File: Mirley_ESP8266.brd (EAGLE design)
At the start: 52 x 69.4 mm, 82 parts, among them J1 61301611121, J10 61300511121, J2 61301611121, J3 61300211121, J6 61300811121, J8 61300811121, T1 BC817U, T10 BC817U, T11 BC817U, T12 BC817U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

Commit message: board chagned
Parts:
- added R57: 47K, rcl:R0805
- moved J8 104.9 mm to (-45.7, 80.0), turned to 0 degrees
- moved J10 102.4 mm to (-64.8, 80.0), turned to 0 degrees
- moved U$4 96.3 mm to (-67.3, 10.2), turned to 0 degrees
- moved R11 79.0 mm to (-16.5, 114.3)
- moved U$1 66.7 mm to (-29.2, 44.5)
- moved ESP_2 66.4 mm to (-33.0, 20.3), turned to 0 degrees
- moved J6 64.2 mm to (-24.1, 80.0), turned to 0 degrees
- moved J2 46.6 mm to (2.62, 33.2), flipped to the top
- moved J1 46.5 mm to (49.1, 33.0), flipped to the top
- moved R59 6.35 mm to (-80.0, 108.0)
- moved C3 6.35 mm to (-29.2, 114.3)
- moved C1 6.35 mm to (-22.9, 114.3)
- moved C2 6.35 mm to (-34.3, 114.3)
- moved C4 6.35 mm to (-39.4, 114.3)
- moved R1 6.35 mm to (-91.4, 108.0)
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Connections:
- removed net N$10: J10.1
- net +3V3: now also R57.2
- net ENABLE: now also J10.2
- net GND: no longer J10.2
- net RESET: now also J10.1
- net TXD: now also R57.1

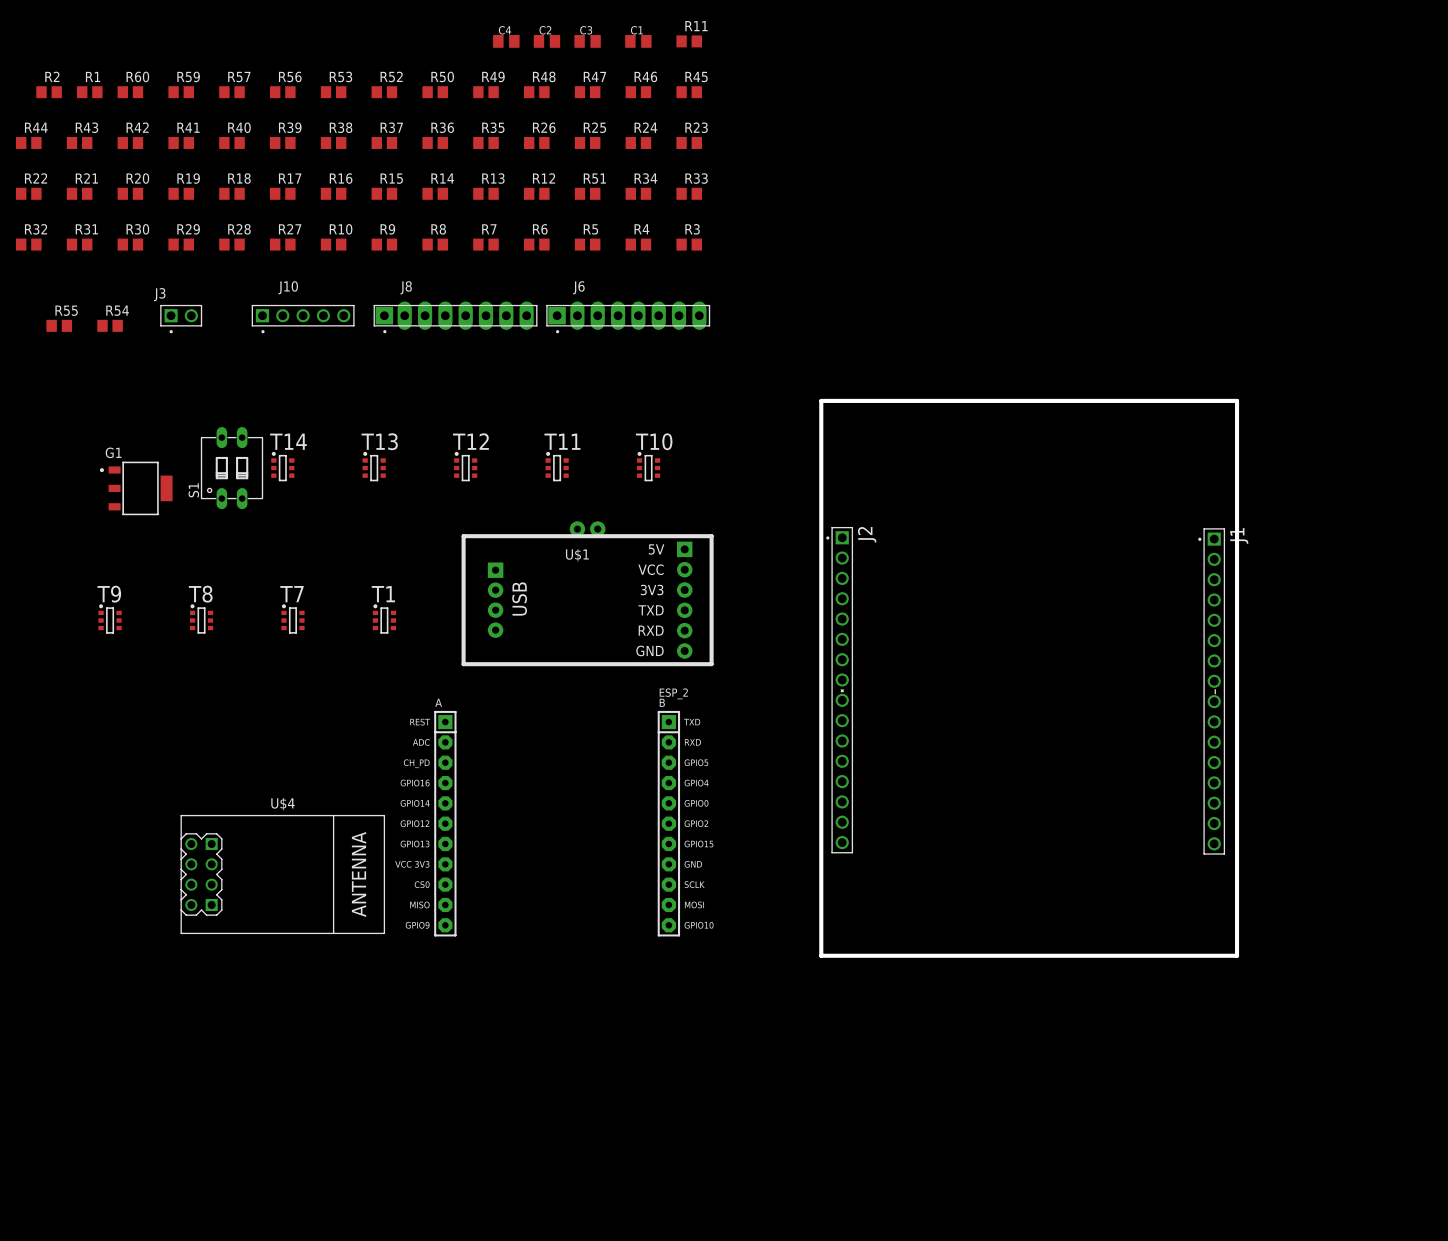
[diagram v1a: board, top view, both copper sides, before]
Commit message: pierwsza wersja na jedenj plytce, niedokonczona
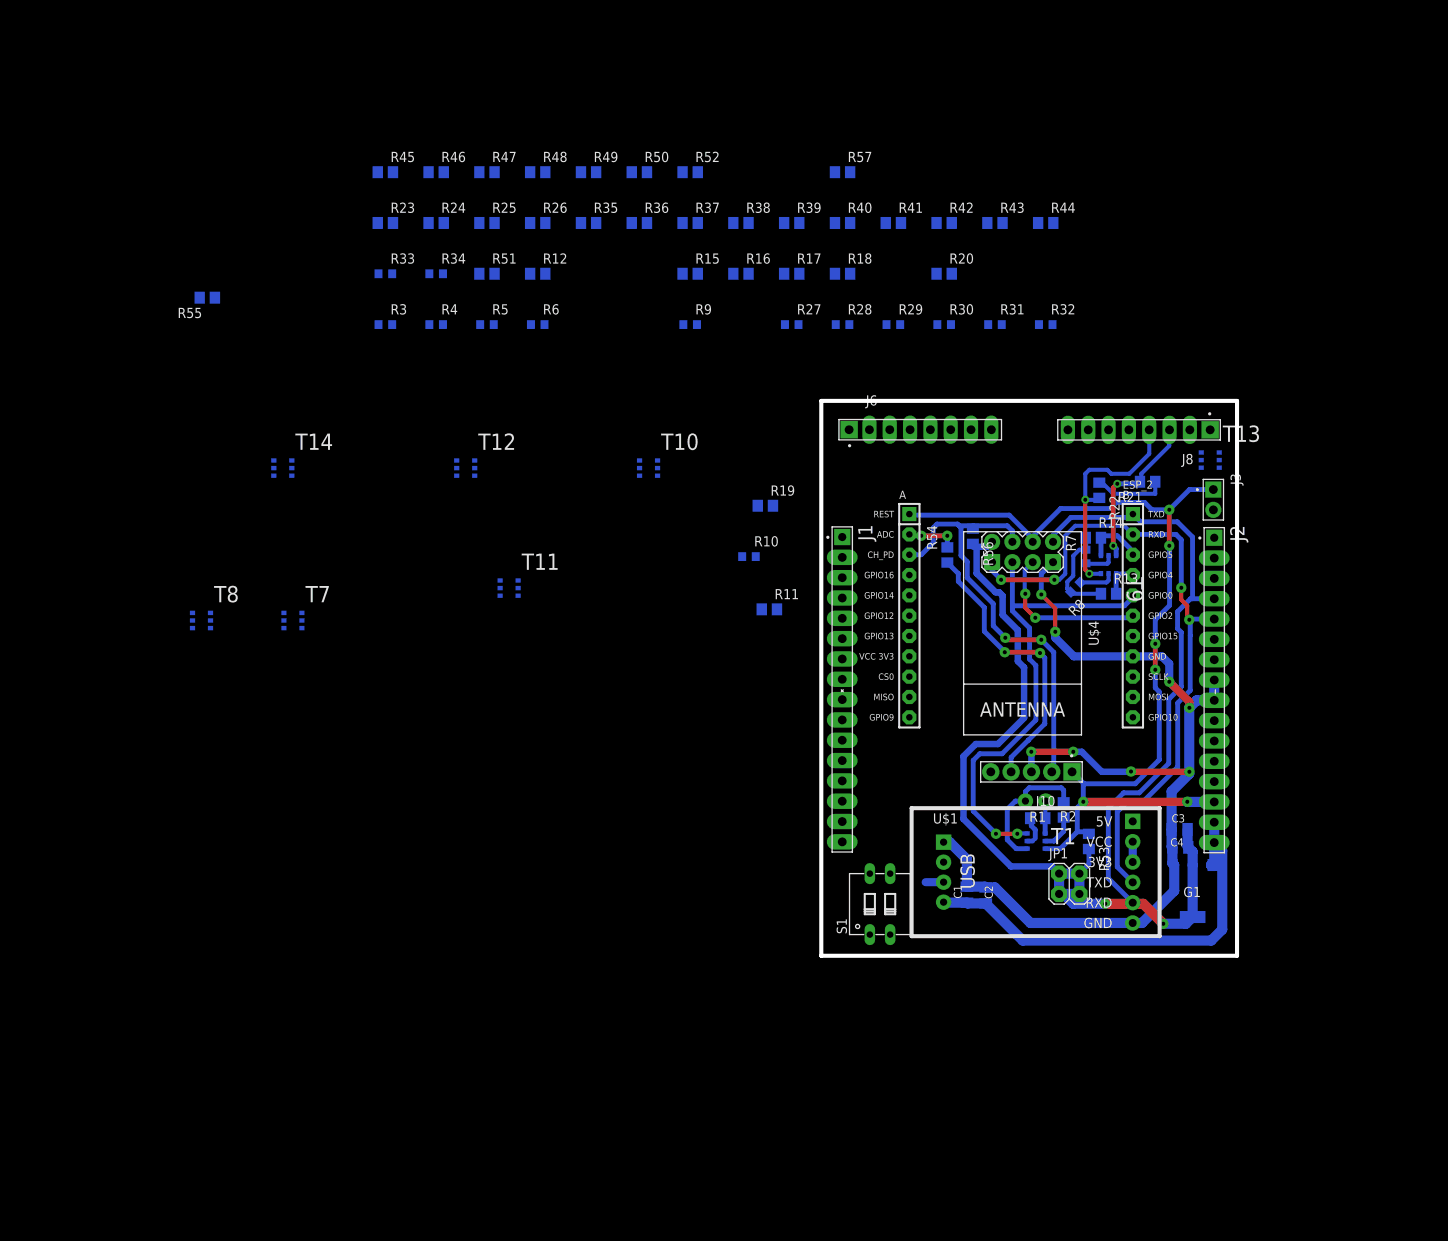
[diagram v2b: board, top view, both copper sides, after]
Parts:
- removed R59, R60: 10K, rcl:R0805
- added JP1: (no value), pinhead:2X02
- R10, R27, R28, R29, R3, R30, R31, R32, R33, R34, R4, R5, R6, R7, R8, R9: device rcl:R0805 -> rcl:R0603
- moved R2 155.3 mm to (30.3, 18.2), flipped to the bottom, turned to 90 degrees
- moved R1 149.3 mm to (27.1, 17.2), flipped to the bottom
- moved G1 140.8 mm to (46.4, 8.09), flipped to the bottom, turned to 270 degrees
- moved R22 138.8 mm to (34.8, 58.2), flipped to the bottom, turned to 90 degrees
- moved R21 138.3 mm to (40.8, 59.2), flipped to the bottom, turned to 180 degrees
- moved R53 133.0 mm to (33.5, 14.3), flipped to the bottom, turned to 90 degrees
- moved C4 131.3 mm to (44.9, 13.6), flipped to the bottom
- moved J3 131.1 mm to (49.0, 57.0), turned to 270 degrees
- moved R32 127.5 mm to (28.1, 78.9), flipped to the bottom
- moved R44 127.5 mm to (28.1, 91.6), flipped to the bottom
- moved T9 125.0 mm to (35.9, 48.9), flipped to the bottom, turned to 90 degrees
- moved C3 123.2 mm to (44.8, 15.8), flipped to the bottom
- moved C2 120.0 mm to (20.6, 7.54), flipped to the bottom, turned to 90 degrees
- moved R31 114.9 mm to (21.7, 78.9), flipped to the bottom
- moved R43 114.9 mm to (21.7, 91.6), flipped to the bottom
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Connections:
- removed net ACD0: ESP_2.2
- removed net ADC0: J10.4, R54.1, R54.2, R55.2
- new net ADC: ESP_2.2, R54.1, R55.2
- new net N$10: J10.4, R54.2
- new net N$5: U$1.3V3, U$1.VCC
- net +3V3: now also JP1.1, JP1.2, JP1.3, JP1.4; no longer R59.1, R60.1
- net ENABLE: no longer R60.2
- net RESET: no longer R59.2
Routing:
- net GND: track 0.00 -> 124.5 mm, vias 0 -> 8
- net RESET: track 0.00 -> 117.0 mm, vias 0 -> 6
- net +3V3: track 0.00 -> 115.2 mm, vias 0 -> 2
- net RXD: track 0.00 -> 85.6 mm, vias 0 -> 4
- net TXD: track 0.00 -> 76.3 mm
- net +5V: track 0.00 -> 66.5 mm
- net GPIO0: track 0.00 -> 60.9 mm, vias 0 -> 2
- net ENABLE: track 0.00 -> 55.9 mm, vias 0 -> 2
- net N$10: track 0.00 -> 35.5 mm, vias 0 -> 2
- net SCL: track 0.00 -> 29.0 mm, vias 0 -> 2
- net GPIO2: track 0.00 -> 20.9 mm, vias 0 -> 2
- net SDA: track 0.00 -> 20.3 mm, vias 0 -> 2
- net RTS: track 0.00 -> 17.3 mm
- net GPIO5: track 0.00 -> 7.55 mm
- net ADC: track 0.00 -> 6.57 mm, vias 0 -> 2
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
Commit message: pytlka programoatora w 50% narysowana
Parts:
- removed C1: 100nF, rcl:C0805K
- removed C2, C4: 10uF, rcl:C0805K
- removed G1: (no value), infineon:SOT230P700X170-4N-1
- removed J3: 61300211121, Headers:61300211121
- removed JP1: (no value), pinhead:2X02
- removed R1, R2: 10K, rcl:R0805
- removed R57: 47K, rcl:R0805
- removed T1: BC817U, transistor:INF-SC74
- removed U$1: USB-SERIAL-CH340, diy-modules:USB-SERIAL-CH340
- removed U$4: WIRELESS-WIFI-ESP-01, diy-modules:WIRELESS-WIFI-ESP-01
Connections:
- removed net 5V: U$1.5V
- removed net DTR: R1.1, T1.4, U$1.DTR
- removed net N$1: R2.1, T1.5
- removed net N$2: R1.2, T1.2
- removed net N$5: U$1.3V3, U$1.VCC
- removed net RTS: R2.2, T1.1, U$1.RTS
- net +3V3: now also J2.6, J2.7; no longer C4.1, G1.2, G1.4, JP1.1, JP1.2, JP1.3, JP1.4, R57.2, U$4.D2
- net +5V: no longer C1.1, C2.1, G1.3, U$1.PLUS
- net D+: no longer U$1.D+
- net D-: no longer U$1.D-
- net ENABLE: no longer U$4.C2
- net GND: no longer C1.2, C2.2, C4.2, G1.1, U$1.GND, U$1.MINUS, U$4.A1
- net GPIO0: now also J2.10; no longer T1.3, U$4.C1
- net GPIO16: no longer J3.2
- net GPIO2: no longer U$4.B1
- net RESET: no longer J3.1, T1.6, U$4.B2
- net RXD: no longer U$1.TXD, U$4.D1
- net TXD: no longer R57.1, U$1.RXD, U$4.A2
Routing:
- net GND: track 124.5 -> 71.7 mm
- net +3V3: track 115.2 -> 71.9 mm, vias 2 -> 0
- net RTS: track 17.3 -> 0.00 mm
- net +5V: track 66.5 -> 50.8 mm
- net GPIO0: track 60.9 -> 54.2 mm
- net RESET: track 117.0 -> 111.7 mm
- net TXD: track 76.3 -> 71.1 mm
- net N$1: track 4.55 -> 0.00 mm
- net DTR: track 4.16 -> 0.00 mm
- net N$2: track 4.14 -> 0.00 mm
- net RXD: track 85.6 -> 81.8 mm
- net N$5: track 2.54 -> 0.00 mm
- net D-: track 2.24 -> 0.00 mm
- net GPIO2: track 20.9 -> 19.4 mm
- net ENABLE: track 55.9 -> 54.5 mm

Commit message: programator zrobiony
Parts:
- removed ESP_2: ESP8266-12-WITH-ADAPTER, esp8266_with_adapter:ESP8266-12-ADAPTER
- removed R53, R56: 10K, rcl:R0805
- removed S1: (no value), switch-dil:DIP02YL
- added ESP_1: ESP8266-12-WITH-ADAPTER, esp8266_with_adapter:ESP8266-12-ADAPTER
- added R1, R2: 10K, rcl:R0805
- added S2: (no value), switch-dil:DIP02YL
- moved C3 37.6 mm to (26.8, 48.8)
- moved J10 19.0 mm to (26.3, 42.0)
- moved R8 9.43 mm to (26.8, 54.1), turned to 90 degrees
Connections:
- net +3V3: now also ESP_1.8, R1.1, R2.1; no longer ESP_2.8, R53.1, R56.1
- net ADC: now also ESP_1.2; no longer ESP_2.2
- net ENABLE: now also ESP_1.3, R2.2; no longer ESP_2.3, R56.2
- net GND: now also ESP_1.16; no longer ESP_2.16
- net GPIO0: now also ESP_1.13; no longer ESP_2.13
- net GPIO1: now also S2.1; no longer S1.1
- net GPIO10: now also ESP_1.22; no longer ESP_2.22
- net GPIO11: now also ESP_1.17; no longer ESP_2.17
- net GPIO12: now also ESP_1.6; no longer ESP_2.6
- net GPIO13: now also ESP_1.7; no longer ESP_2.7
- net GPIO14: now also ESP_1.5; no longer ESP_2.5
- net GPIO15: now also ESP_1.15; no longer ESP_2.15
- net GPIO16: now also ESP_1.4; no longer ESP_2.4
- net GPIO2: now also ESP_1.14; no longer ESP_2.14
- net GPIO3: now also S2.2; no longer S1.2
- net GPIO4: now also ESP_1.12; no longer ESP_2.12
- net GPIO5: now also ESP_1.11; no longer ESP_2.11
- net GPIO6: now also ESP_1.20; no longer ESP_2.20
- net GPIO7: now also ESP_1.18; no longer ESP_2.18
- net GPIO8: now also ESP_1.21; no longer ESP_2.21
- net GPIO9: now also ESP_1.19; no longer ESP_2.19
- net RESET: now also ESP_1.1, R1.2; no longer ESP_2.1, R53.2
- net RXD: now also ESP_1.10, S2.3; no longer ESP_2.10, S1.3
- net TXD: now also ESP_1.9, S2.4; no longer ESP_2.9, S1.4
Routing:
- net RESET: track 111.7 -> 0.00 mm, vias 6 -> 0
- net RXD: track 81.8 -> 0.00 mm, vias 4 -> 0
- net GND: track 71.7 -> 0.00 mm, vias 8 -> 0
- net TXD: track 71.1 -> 0.00 mm
- net +3V3: track 71.9 -> 1.90 mm
- net GPIO0: track 54.2 -> 0.00 mm, vias 2 -> 0
- net ENABLE: track 54.5 -> 0.35 mm, vias 2 -> 0
- net +5V: track 50.8 -> 1.43 mm
- net N$10: track 35.5 -> 0.00 mm, vias 2 -> 0
- net SCL: track 29.0 -> 0.35 mm, vias 2 -> 0
- net SDA: track 20.3 -> 0.58 mm, vias 2 -> 0
- net GPIO2: track 19.4 -> 0.00 mm, vias 2 -> 0
- net GPIO5: track 7.55 -> 0.35 mm
- net ADC: track 6.57 -> 0.01 mm, vias 2 -> 0
- net GPIO4: track 4.69 -> 0.00 mm
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
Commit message: usb-uart skonczone, druga skonczona w 50%
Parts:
- removed J10: 61300511121, Headers:61300511121
- removed J6: 61300811121, Headers:61300811121
- added JP1: (no value), pinhead:2X08
- added JP2: (no value), pinhead:1X02
- added JP3: (no value), pinhead:1X03
- J8: value 61300811121 -> (none); device Headers:61300811121 -> pinhead:2X08
- moved R12 118.6 mm to (3.56, -26.8)
- moved R15 118.6 mm to (22.6, -26.8)
- moved R16 118.6 mm to (29.0, -26.8)
- moved R17 118.6 mm to (35.3, -26.8)
- moved R18 118.6 mm to (41.7, -26.8)
- moved R20 118.6 mm to (54.4, -26.8)
- moved R23 118.6 mm to (-15.5, -20.4)
- moved R24 118.6 mm to (-9.14, -20.4)
- moved R25 118.6 mm to (-2.79, -20.4)
- moved R26 118.6 mm to (3.56, -20.4)
- moved R27 118.6 mm to (35.3, -33.1)
- moved R28 118.6 mm to (41.7, -33.1)
- moved R29 118.6 mm to (48.0, -33.1)
- moved R3 118.6 mm to (-15.5, -33.1)
- moved R30 118.6 mm to (54.4, -33.1)
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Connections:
- removed net LED_A4]: J1.12
- removed net N$10: J10.4, R54.2
- removed net N$9: J6.2, R44.1, T7.3
- new net N$1: JP1.3, JP1.4, R44.1, T7.3
- new net N$2: JP3.2, R54.2
- net +3V3: now also J2.5; no longer J2.7
- net ENABLE: now also JP3.1; no longer J10.2
- net GND: now also J2.7; no longer J10.3, J2.9
- net GPIO0: now also J2.9; no longer J2.10
- net GPIO1: now also S2.2; no longer S2.1
- net GPIO16: now also JP2.1, JP2.2; no longer J10.5
- net GPIO3: now also S2.1; no longer S2.2
- net LED_A1: now also JP1.11, JP1.12; no longer J6.6
- net LED_A2: now also JP1.10, JP1.9; no longer J6.5
- net LED_A3: now also JP1.7, JP1.8; no longer J6.4
- net LED_A4: now also J1.12, JP1.5, JP1.6; no longer J6.3
- net LL1: now also J8.2
- net LL2: now also J8.3, J8.4; no longer J8.2
- net LL3: now also J8.10, J8.9; no longer J8.5
- net LL4: now also J8.11, J8.12; no longer J8.6
- net LL5: now also J8.13, J8.14; no longer J8.7
- net LL6: now also J8.15, J8.16; no longer J8.8
- net LL7: now also JP1.15, JP1.16; no longer J6.8
- net LL8: now also JP1.13, JP1.14; no longer J6.7
- net N$3: now also JP1.1, JP1.2; no longer J6.1
- net RESET: now also J2.10, JP3.3; no longer J10.1
- net RXD: now also ESP_1.9, J2.4; no longer ESP_1.10, J2.5
- net SCL: now also J8.7, J8.8; no longer J8.4
- net SDA: now also J8.5, J8.6; no longer J8.3
- net TXD: now also ESP_1.10, J2.3; no longer ESP_1.9, J2.4
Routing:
- net GND: track 0.00 -> 90.0 mm, vias 0 -> 2
- net +5V: track 1.43 -> 89.1 mm, vias 0 -> 6
- net LED_A4: track 0.00 -> 81.6 mm, vias 0 -> 2
- net LED_A3: track 0.00 -> 73.8 mm, vias 0 -> 2
- net RESET: track 0.00 -> 68.3 mm, vias 0 -> 2
- net LED_A2: track 0.00 -> 59.1 mm, vias 0 -> 2
- net SDA: track 0.58 -> 54.8 mm, vias 0 -> 2
- net LED_A1: track 0.00 -> 52.7 mm, vias 0 -> 2
- net SCL: track 0.35 -> 51.2 mm, vias 0 -> 2
- net LL8: track 0.00 -> 36.6 mm, vias 0 -> 2
- net ADC: track 0.01 -> 36.5 mm, vias 0 -> 2
- net N$3: track 0.00 -> 36.3 mm
- net N$1: track 0.00 -> 34.2 mm
- net TXD: track 0.00 -> 29.8 mm
- net LL7: track 0.00 -> 28.0 mm, vias 0 -> 2
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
